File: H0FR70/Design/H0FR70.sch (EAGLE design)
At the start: 39 parts, among them P2 HEXABIT_17.32_NO_P6_P7_P12, Q1 BSS123, Q2 STD36P4LLF6, U2 INA199A2DCKT, X1 XTALL_CSTCE8M00G52

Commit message: OUTPUT files were added
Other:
- note added: "2V_10A"
- note added: "D4"
- moved on the sheet: C10, C11, C12, C13, D3, Q1, Q2, R10, R12, R4, R5, R6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

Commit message: Zener was deleted prooerties was changed to 12V 20A
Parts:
- removed D4: BZT52C2V0S-7-F, Hexabitz:BZT52C2V0S-7-F
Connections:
- net AGND: no longer D4.1
- net N$7: no longer D4.2
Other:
- note added: "SPST MOSFET Switch 20A 12V"
- note added: "V_load=(3.3-12)"
- note removed: "2V_10A"
- note removed: "D4"
- note removed: "SPST MOSFET Switch 20A 40V"
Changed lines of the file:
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@@
 <?xml version="1.0" encoding="utf-8"?>
 <!DOCTYPE eagle SYSTEM "eagle.dtd">
-<eagle version="9.6.0">
+<eagle version="9.6.1">
 <drawing>
 <settings>
@@
 <part name="SUPPLY14" library="supply2" deviceset="VCC" device="" value="VDDA"/>
 <part name="X2" library="con-ptr500" library_urn="urn:adsk.eagle:library:181" deviceset="AK500/3" device="" package3d_urn="urn:adsk.eagle:package:9883/1"/>
-<part name="SUPPLY15" library="supply2" deviceset="AGND" device="" value="VSSA"/>
 <part name="R12" library="Hexabitz" deviceset="R-0603" device="" value="10.0K">
 <attribute name="MFN" value="Yageo"/>
@@
 <attribute name="RESISTANCE" value="0.0 Ohm"/>
 </part>
-<part name="D4" library="Hexabitz" deviceset="BZT52C2V0S-7-F" device="">
-<attribute name="DESCRIPTION" value="BZT52C2V0S Series 2 V 10 mA Surface Mount Zener Diode - SOD-323"/>
-<attribute name="MFN" value="Diodes Inc."/>
-<attribute name="MPN" value="BZT52C2V0S-7-F"/>
-<attribute name="OCTOPART_URL" value="https://octopart.com/bzt52c2v0s-7-f-diodes+inc.-7151792?r=sp"/>
-</part>
 </parts>
 <sheets>
@@
 <wire x1="231.14" y1="18.288" x2="231.14" y2="22.86" width="0.1524" layer="205"/>
 <text x="242.6462" y="6.1722" size="1.9304" layer="100" font="vector">www.hexabitz.com</text>
-<text x="170.3578" y="11.2014" size="1.9304" layer="101" font="vector">SPST MOSFET Switch  20A 40V</text>
+<text x="170.3578" y="11.2014" size="1.9304" layer="101" font="vector">SPST MOSFET Switch  20A 12V</text>
 <text x="181.8278" y="5.0114" size="1.9304" layer="101" font="vector">Amir Tabbakh</text>
 <text x="27.94" y="198.12" size="1.778" layer="150">VDD=3.3 Volts</text>
@@
 <text x="199.4662" y="19.6342" size="1.9304" layer="100" font="vector">Title</text>
 <text x="180.9242" y="19.6342" size="1.9304" layer="102" font="vector">H0FR7</text>
-<text x="170.3578" y="11.2014" size="1.9304" layer="101" font="vector">SPST MOSFET Switch  20A 40V</text>
+<text x="170.3578" y="11.2014" size="1.9304" layer="101" font="vector">SPST MOSFET Switch  20A 12V</text>
 <text x="206.3242" y="19.6342" size="1.9304" layer="101" font="vector">H0FR7_Frontend</text>
 <wire x1="168.91" y1="3.81" x2="168.91" y2="8.128" width="0.1524" layer="205"/>
@@
 <text x="34.29" y="68.58" size="2.1844" layer="150">Power and Load Connector</text>
 <text x="189.23" y="102.87" size="1.778" layer="150">Gain = 100 V/V</text>
-<text x="124.46" y="119.38" size="1.778" layer="95">D4</text>
-<text x="124.46" y="114.3" size="1.778" layer="95">2V_10A</text>
+<text x="143.51" y="168.91" size="1.778" layer="150">V_load=(3.3-12)</text>
 </plain>
 <instances>
@@
 <attribute name="VALUE" x="64.77" y="44.577" size="1.778" layer="96" rot="MR0"/>
 </instance>
-<instance part="SUPPLY15" gate="G$1" x="120.65" y="92.71" smashed="yes">
-<attribute name="VALUE" x="121.285" y="84.963" size="1.778" layer="96" rot="R90"/>
-</instance>
 <instance part="R12" gate="G$1" x="52.07" y="129.54" smashed="yes" rot="R180">
 <attribute name="NAME" x="48.26" y="132.3086" size="1.778" layer="95"/>
@@
 <attribute name="VALUE" x="125.73" y="140.208" size="1.778" layer="96"/>
 </instance>
-<instance part="D4" gate="G$1" x="120.65" y="118.11" smashed="yes" rot="R90">
-<attribute name="DESCRIPTION" x="120.65" y="118.11" size="1.778" layer="96" rot="R90" display="off"/>
-<attribute name="MFN" x="120.65" y="118.11" size="1.778" layer="96" rot="R90" display="off"/>
-<attribute name="MPN" x="120.65" y="118.11" size="1.778" layer="96" rot="R90" display="off"/>
-<attribute name="OCTOPART_URL" x="120.65" y="118.11" size="1.778" layer="96" rot="R90" display="off"/>
-</instance>
 </instances>
 <busses>
@@
 <pinref part="R4" gate="G$1" pin="2"/>
 <pinref part="R6" gate="G$1" pin="2"/>
-<pinref part="D4" gate="G$1" pin="2"/>
-<wire x1="120.65" y1="124.46" x2="120.65" y2="143.51" width="0.1524" layer="91"/>
 </segment>
 </net>
@@
 <pinref part="D2" gate="G$1" pin="C"/>
 </segment>
-<segment>
-<pinref part="SUPPLY15" gate="G$1" pin="AGND"/>
-<pinref part="D4" gate="G$1" pin="1"/>
-<wire x1="120.65" y1="110.49" x2="120.65" y2="95.25" width="0.1524" layer="91"/>
-</segment>
 </net>

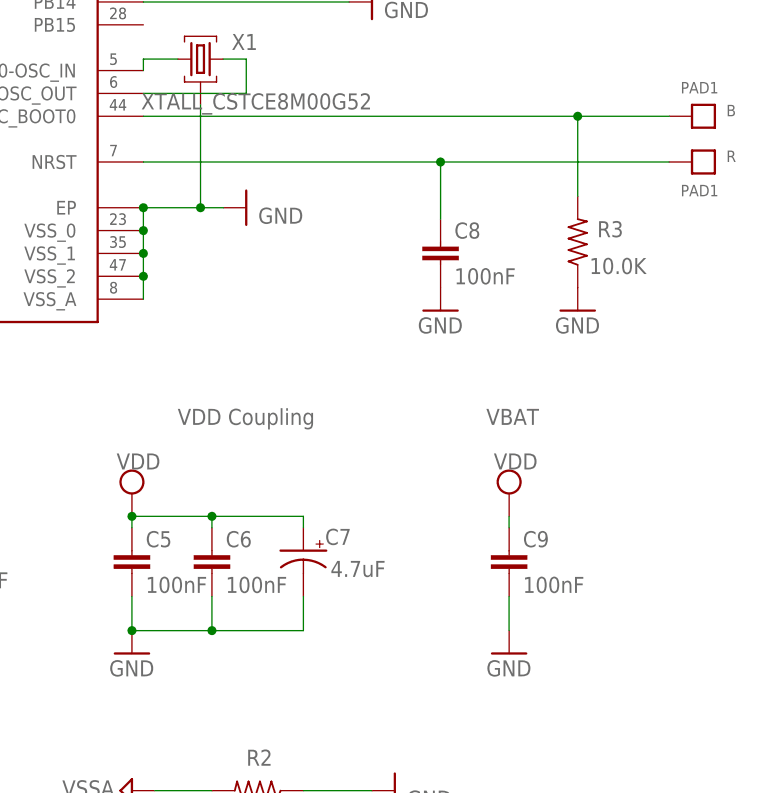
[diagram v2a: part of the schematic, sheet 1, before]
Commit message: PDF fixed R8 changed (2k2 -> 1k) BOM modified
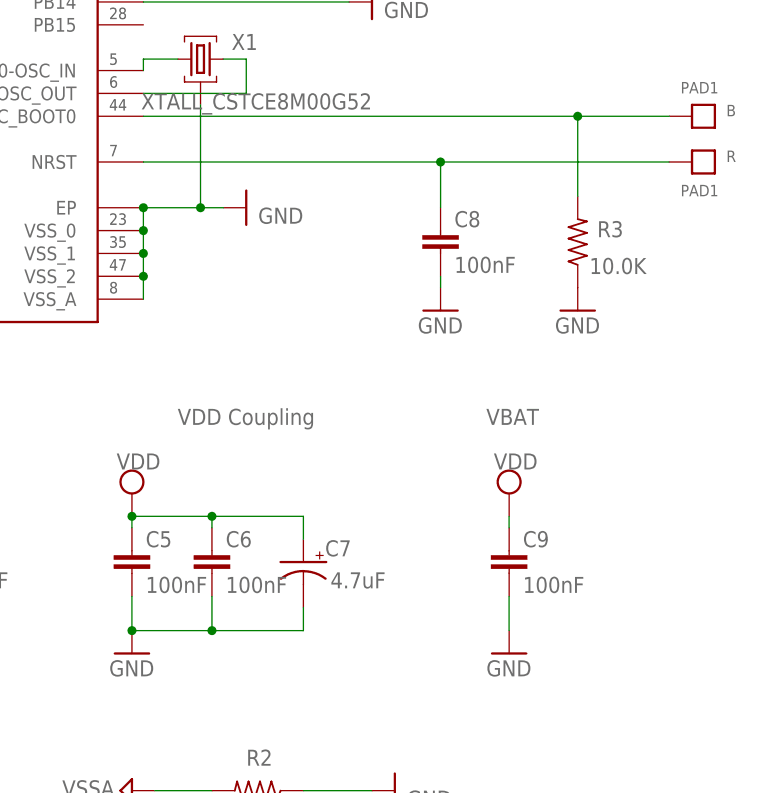
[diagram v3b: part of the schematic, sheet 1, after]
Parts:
- B, C, D, R: device Hexabitz:PAD1 -> HEXABITZ_CONNECTION_PARTS:PAD1
- C1, C11, C12, C13, C3, C5, C6, C8, C9: device Hexabitz:C-0603 -> HEXABITZ_RCLS:C-0603
- C10, C2, C4, C7: device Hexabitz:C-0805-POL -> HEXABITZ_RCLS:C-0805-POL
- D1: device Hexabitz:VLMS1300-GS08 -> HEXABITZ_USER_INTERFACE_PARTS:VLMS1300-GS08
- D2: value ORANGE -> Orange; device Hexabitz:VLMS1300-GS08 -> HEXABITZ_USER_INTERFACE_PARTS:VLMS1300-GS08
- D3: device Hexabitz:SMD-DIODE-SCHOTTKY-40V-300MA(SOD-323) -> HEXABITZ_RCLS:SMD-DIODE-SCHOTTKY-40V-300MA(SOD-323)
- FB1: device Hexabitz:FB-TDK_MMZ1608Y300B -> HEXABITZ_RCLS:FB-TDK_MMZ1608Y300B
- Q1: device Hexabitz:BSS123 -> HEXABITZ_RCLS:BSS123
- Q2: device Hexabitz:STD36P4LLF6 -> HEXABITZ_RCLS:STD36P4LLF6
- R1, R10, R12, R2, R3, R4, R5, R6, R8: device Hexabitz:R-0603 -> HEXABITZ_RCLS:R-0603
- R7: device Hexabitz:R-US_R2512 -> HEXABITZ_RCLS:R-US_R2512
- U1: device Hexabitz:STM32F091CBU6 -> HEXABITZ_ICs:STM32F091CBU6
- U2: device Hexabitz:INA199A2DCKT -> HEXABITZ_ICs:INA199A2DCKT
- X1: device Hexabitz:XTALL_CSTCE8M00G52 -> HEXABITZ_OTHER_PARTS:XTALL_CSTCE8M00G52
- X2: device con-ptr500:AK500/3 -> HEXABITZ_CONNECTION_PARTS:AK500/3
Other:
- moved on the sheet: C7, C8

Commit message: no message
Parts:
- D2: value Orange -> RED
- R8: value 2k2 -> 1k; MPN RC0603FR-07270RL -> RC0603JR-071KL; OCTOPART_URL https://octopart.com/search?q=RC0603FR-07270RL&start=0 -> https://octopart.com/rc0603jr-071kl-yageo-55402888?r=sp; RESISTANCE 270.0 Ohm -> 1k
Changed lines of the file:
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@@
 <setting verticaltext="up"/>
 </settings>
-<grid distance="50" unitdist="mil" unit="mil" style="lines" multiple="1" display="no" altdistance="0.01" altunitdist="inch" altunit="inch"/>
+<grid distance="0.1" unitdist="inch" unit="inch" style="lines" multiple="1" display="no" altdistance="0.01" altunitdist="inch" altunit="inch"/>
 <layers>
 <layer number="1" name="Top" color="4" fill="1" visible="no" active="no"/>
@@
 <part name="P2" library="hexabitz_connectors" library_urn="urn:adsk.eagle:library:20064578" deviceset="HEXABIT_?_NO_P6_P7_P12" device="17.32" package3d_urn="urn:adsk.eagle:package:20064634/2"/>
 <part name="GND15" library="supply1" library_urn="urn:adsk.eagle:library:371" deviceset="GND" device=""/>
-<part name="R8" library="HEXABITZ_RCLS" library_urn="urn:adsk.eagle:library:20064561" deviceset="R-0603" device="" package3d_urn="urn:adsk.eagle:package:1435818/3" value="2k2">
-<attribute name="MFN" value="Yageo"/>
-<attribute name="MPN" value="RC0603FR-07270RL"/>
-<attribute name="OCTOPART_URL" value="https://octopart.com/search?q=RC0603FR-07270RL&amp;start=0"/>
-<attribute name="RESISTANCE" value="270.0 Ohm"/>
+<part name="R8" library="HEXABITZ_RCLS" library_urn="urn:adsk.eagle:library:20064561" deviceset="R-0603" device="" package3d_urn="urn:adsk.eagle:package:1435818/3" value="1k">
+<attribute name="MFN" value="Yageo"/>
+<attribute name="MPN" value="RC0603JR-071KL"/>
+<attribute name="OCTOPART_URL" value="https://octopart.com/rc0603jr-071kl-yageo-55402888?r=sp"/>
+<attribute name="RESISTANCE" value="1k"/>
 <attribute name="TOLERANCE" value="1%"/>
 </part>
 <part name="SUPPLY1" library="supply2" deviceset="AGND" device="" value="VSSA"/>
-<part name="D2" library="HEXABITZ_USER_INTERFACE_PARTS" library_urn="urn:adsk.eagle:library:20064563" deviceset="VLMS1300-GS08" device="" package3d_urn="urn:adsk.eagle:package:20064571/2" value="Orange">
+<part name="D2" library="HEXABITZ_USER_INTERFACE_PARTS" library_urn="urn:adsk.eagle:library:20064563" deviceset="VLMS1300-GS08" device="" package3d_urn="urn:adsk.eagle:package:20064571/2" value="RED">
 <attribute name="MFN" value="Vishay"/>
 <attribute name="MPN" value="VLMO1300-GS08 "/>
